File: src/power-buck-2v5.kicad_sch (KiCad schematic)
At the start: 12 parts, among them U16 INA219xxDCN, U3 TPS562202DRLR

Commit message: Start placing the power monitoring
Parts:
- C154: footprint Capacitor_SMD:C_0201_0603Metric -> Capacitor_SMD:C_0402_1005Metric
- R41: footprint (none) -> Resistor_SMD:R_0805_2012Metric
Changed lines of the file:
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@@
 			)
 		)
-		(property "Footprint" ""
+		(property "Footprint" "Resistor_SMD:R_0805_2012Metric"
 			(at 190.5 86.868 90)
 			(effects
@@
 			)
 		)
-		(property "Footprint" "Capacitor_SMD:C_0201_0603Metric"
+		(property "Footprint" "Capacitor_SMD:C_0402_1005Metric"
 			(at 257.81 86.36 0)
 			(effects

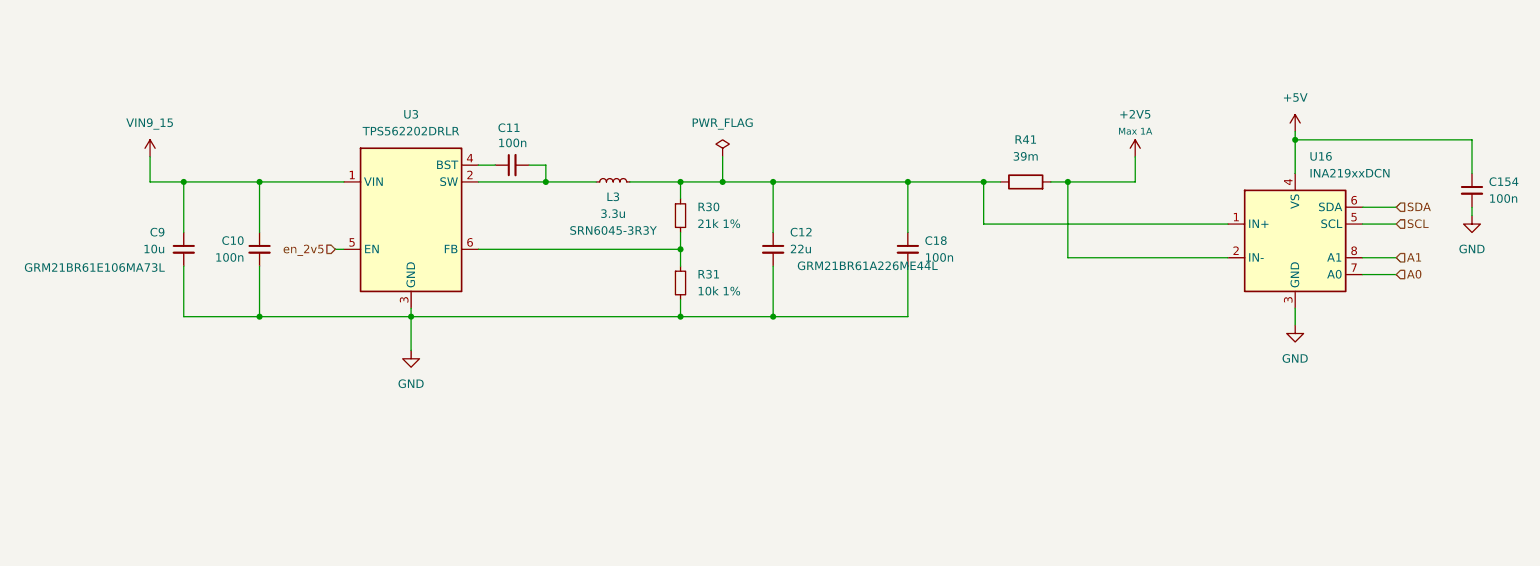
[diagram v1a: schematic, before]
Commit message: Add routing of the io connector gnd pins
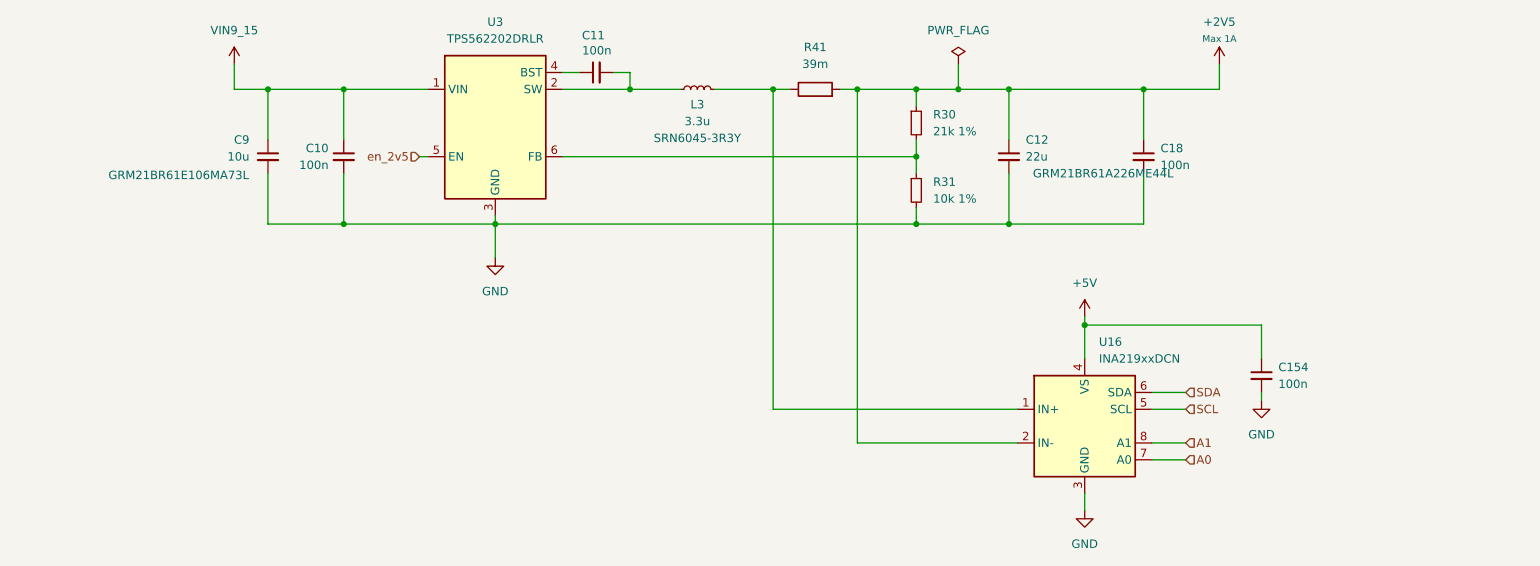
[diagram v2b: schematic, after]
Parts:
- R41: footprint Resistor_SMD:R_0805_2012Metric -> Resistor_SMD:R_1206_3216Metric
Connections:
- net +2V5: now also C12.1, C18.1, R30.1
- net at L3.2, R41.1, U16.1 (IN+): no longer C12.1, C18.1, R30.1
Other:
- moved on the sheet: C10, C11, C12, C154, C18, C9, L3, R30, R31, R41, U16, U3
